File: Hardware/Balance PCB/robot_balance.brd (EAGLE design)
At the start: 100 x 50 mm, 49 parts, among them Q1 16Mhz

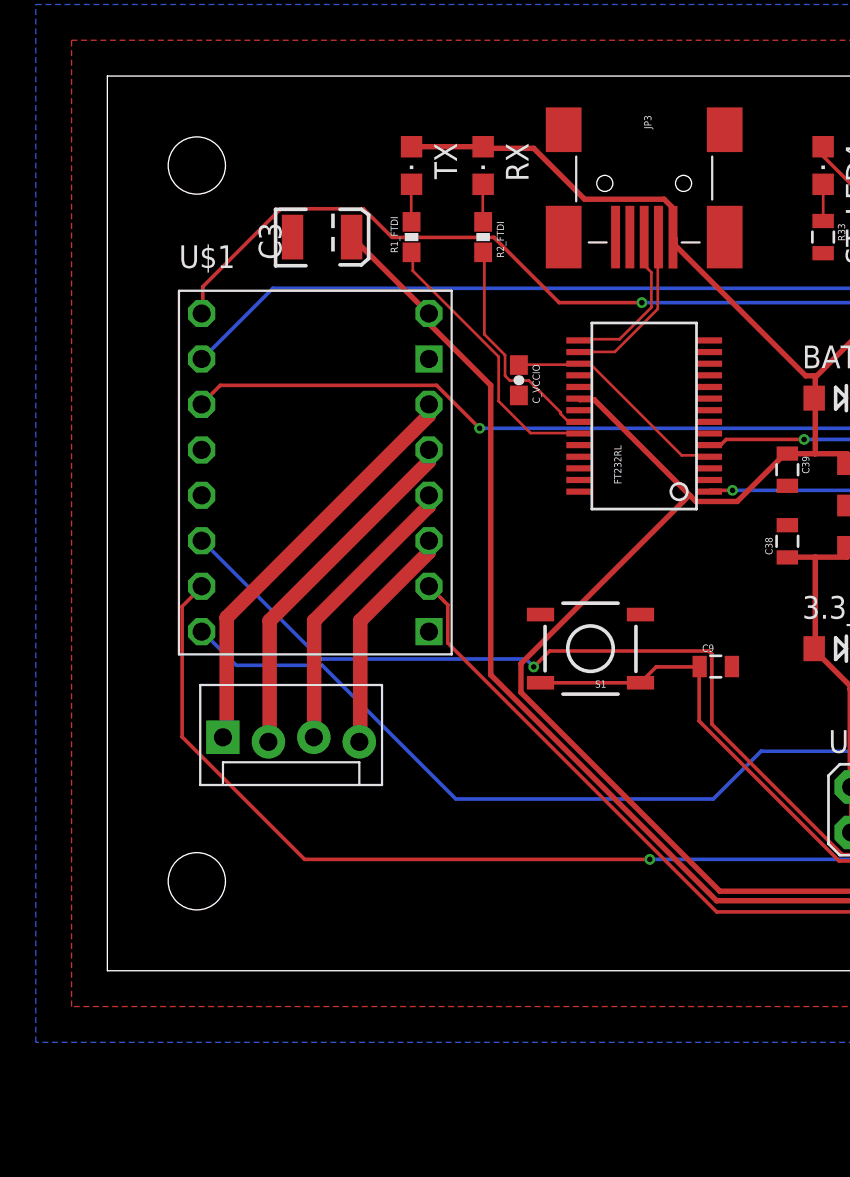
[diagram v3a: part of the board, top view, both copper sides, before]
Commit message: Micro usb instead of Mini
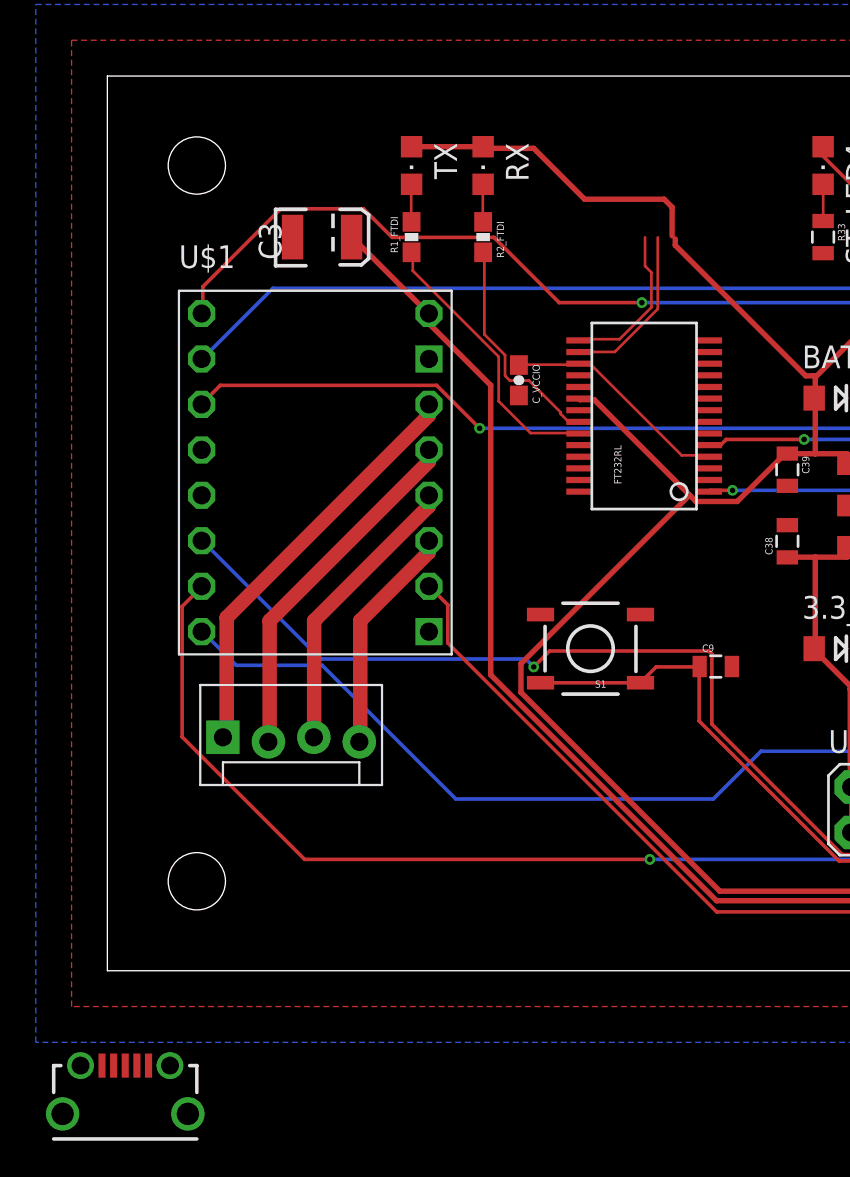
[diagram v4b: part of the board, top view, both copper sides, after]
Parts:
- removed JP3: USBOLD, SparkFun-Connectors:USB-MINIB-OLD
- added P1: 10118194-0001LF, usb_micro:10118194-0001LF
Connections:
- net 5V: now also P1.1; no longer JP3.VBUS
- net GND: now also P1.M1, P1.M2, P1.M3, P1.M4; no longer JP3.GND
- net USB_D+: now also P1.3; no longer JP3.D+
- net USB_D-: now also P1.2; no longer JP3.D-
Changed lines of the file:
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@@
 <attribute name="PROD_ID" value="CAP-08310" x="51.63" y="65.13" size="1.778" layer="27" display="off"/>
 </element>
-<element name="JP3" library="SparkFun-Connectors" package="USB-MINIB-OLD" value="USBOLD" x="30" y="44" rot="R270"/>
 <element name="JP4" library="SparkFun-Connectors" package="MOLEX-1X4_LOCK" value="" x="68" y="44" rot="R180"/>
 <element name="JP5" library="SparkFun-Connectors" package="MOLEX-1X4_LOCK" value="" x="72" y="6"/>
@@
 <element name="C_VCCIO" library="SparkFun-Capacitors" package="0603-CAP" value="0.1uF" x="23" y="33" rot="R270"/>
 <element name="U$2" library="JonathanLukas" package="2X10" value="JTAG_20PIN" x="53" y="9"/>
+<element name="P1" library="usb_micro" package="10118194-0001LF" value="10118194-0001LF" x="1" y="-8">
+<attribute name="MANPARTNO" value="10118194-0001LF" x="1" y="-8" size="1.778" layer="27" display="off"/>
+<attribute name="DISTRIBUTOR" value="Digikey" x="1" y="-8" size="1.778" layer="27" display="off"/>
+<attribute name="PARTNO" value="GT10040" x="1" y="-8" size="1.778" layer="27" display="off"/>
+<attribute name="MANUFACTURER" value="FCI" x="1" y="-8" size="1.778" layer="27" display="off"/>
+<attribute name="POPULATE" value="yes" x="1" y="-8" size="1.778" layer="27" display="off"/>
+<attribute name="DISTPARTNO" value="609-4618-1-ND" x="1" y="-8" size="1.778" layer="27" display="off"/>
+</element>
 </elements>
 <signals>
@@
 <vertex x="-2" y="-2"/>
 </polygon>
-<contactref element="JP3" pad="GND"/>
 <polygon width="0.1524" layer="16">
 <vertex x="-4" y="54"/>
@@
 <contactref element="U$2" pad="6"/>
 <contactref element="U$2" pad="4"/>
+<contactref element="P1" pad="M2"/>
+<contactref element="P1" pad="M4"/>
+<contactref element="P1" pad="M1"/>
+<contactref element="P1" pad="M3"/>
+<wire x1="86.81" y1="41" x2="94.97" y2="34.19" width="0" layer="19" extent="1-1"/>
+<wire x1="94.97" y1="18.95" x2="94.97" y2="34.19" width="0" layer="19" extent="1-1"/>
+<wire x1="76.9" y1="29" x2="86.81" y2="41" width="0" layer="19" extent="1-1"/>
+<wire x1="76.9" y1="26" x2="76.9" y2="29" width="0" layer="19" extent="1-1"/>
+<wire x1="72" y1="35.9" x2="76.9" y2="29" width="0" layer="19" extent="1-1"/>
+<wire x1="63" y1="35.9" x2="72" y2="35.9" width="0" layer="19" extent="1-1"/>
+<wire x1="62.75" y1="30.8" x2="63" y2="35.9" width="0" layer="19" extent="1-1"/>
+<wire x1="60.15" y1="23.25" x2="62.75" y2="30.8" width="0" layer="19" extent="1-1"/>
+<wire x1="62.75" y1="19.2" x2="60.15" y2="23.25" width="0" layer="19" extent="1-1"/>
 <wire x1="63" y1="15.1" x2="62.75" y2="19.2" width="0" layer="19" extent="1-1"/>
+<wire x1="66" y1="15.1" x2="63" y2="15.1" width="0" layer="19" extent="1-1"/>
 <wire x1="70" y1="15.1" x2="66" y2="15.1" width="0" layer="19" extent="1-1"/>
-<wire x1="60.15" y1="23.25" x2="62.75" y2="19.2" width="0" layer="19" extent="1-1"/>
+<wire x1="73" y1="15.1" x2="70" y2="15.1" width="0" layer="19" extent="1-1"/>
 <wire x1="61.89" y1="10.27" x2="63" y2="15.1" width="0" layer="19" extent="1-1"/>
-<wire x1="62.75" y1="30.8" x2="63" y2="35.9" width="0" layer="19" extent="1-1"/>
-<wire x1="23" y1="32.15" x2="17.97" y2="34.19" width="0" layer="19" extent="1-1"/>
-<wire x1="26.344" y1="31.325" x2="23" y2="32.15" width="0" layer="19" extent="1-1"/>
+<wire x1="64.43" y1="10.27" x2="61.89" y2="10.27" width="0" layer="19" extent="1-1"/>
+<wire x1="59.35" y1="10.27" x2="61.89" y2="10.27" width="0" layer="19" extent="1-1"/>
+<wire x1="56.81" y1="10.27" x2="59.35" y2="10.27" width="0" layer="19" extent="1-1"/>
+<wire x1="54.27" y1="10.27" x2="56.81" y2="10.27" width="0" layer="19" extent="1-1"/>
+<wire x1="51.73" y1="10.27" x2="54.27" y2="10.27" width="0" layer="19" extent="1-1"/>
+<wire x1="49.19" y1="10.27" x2="51.73" y2="10.27" width="0" layer="19" extent="1-1"/>
+<wire x1="46.65" y1="10.27" x2="49.19" y2="10.27" width="0" layer="19" extent="1-1"/>
+<wire x1="44.11" y1="10.27" x2="46.65" y2="10.27" width="0" layer="19" extent="1-1"/>
+<wire x1="55.1" y1="18" x2="60.15" y2="23.25" width="0" layer="19" extent="1-1"/>
+<wire x1="53" y1="20.1" x2="55.1" y2="18" width="0" layer="19" extent="1-1"/>
+<wire x1="52.2" y1="24.9" x2="53" y2="20.1" width="0" layer="19" extent="1-1"/>
+<wire x1="53.8" y1="27.1" x2="52.2" y2="24.9" width="0" layer="19" extent="1-1"/>
+<wire x1="53" y1="31.9" x2="53.8" y2="27.1" width="0" layer="19" extent="1-1"/>
+<wire x1="47.9" y1="32" x2="53" y2="31.9" width="0" layer="19" extent="1-1"/>
+<wire x1="47.9" y1="18" x2="53" y2="20.1" width="0" layer="19" extent="1-1"/>
+<wire x1="48" y1="40.1" x2="47.9" y2="32" width="0" layer="19" extent="1-1"/>
+<wire x1="52" y1="40.1" x2="48" y2="40.1" width="0" layer="19" extent="1-1"/>
+<wire x1="44" y1="40.1" x2="48" y2="40.1" width="0" layer="19" extent="1-1"/>
+<wire x1="40" y1="40.1" x2="44" y2="40.1" width="0" layer="19" extent="1-1"/>
+<wire x1="41.9012" y1="26" x2="47.9" y2="32" width="0" layer="19" extent="1-1"/>
+<wire x1="38" y1="27.1" x2="41.9012" y2="26" width="0" layer="19" extent="1-1"/>
+<wire x1="38" y1="24.9" x2="38" y2="27.1" width="0" layer="19" extent="1-1"/>
+<wire x1="33.656" y1="30.675" x2="38" y2="27.1" width="0" layer="19" extent="1-1"/>
+<wire x1="26.344" y1="31.325" x2="33.656" y2="30.675" width="0" layer="19" extent="1-1"/>
 <wire x1="26.344" y1="33.275" x2="26.344" y2="31.325" width="0" layer="19" extent="1-1"/>
 <wire x1="26.344" y1="28.725" x2="26.344" y2="31.325" width="0" layer="19" extent="1-1"/>
+<wire x1="26.344" y1="28.075" x2="26.344" y2="28.725" width="0" layer="19" extent="1-1"/>
+<wire x1="23" y1="32.15" x2="26.344" y2="31.325" width="0" layer="19" extent="1-1"/>
+<wire x1="17.97" y1="34.19" x2="23" y2="32.15" width="0" layer="19" extent="1-1"/>
+<wire x1="24.206" y1="19.905" x2="26.344" y2="28.075" width="0" layer="19" extent="1-1"/>
 <wire x1="29.794" y1="19.905" x2="24.206" y2="19.905" width="0" layer="19" extent="1-1"/>
-<wire x1="44" y1="40.1" x2="48" y2="40.1" width="0" layer="19" extent="1-1"/>
-<wire x1="53" y1="31.9" x2="47.9" y2="32" width="0" layer="19" extent="1-1"/>
-<wire x1="53.8" y1="27.1" x2="53" y2="31.9" width="0" layer="19" extent="1-1"/>
-<wire x1="33.656" y1="30.675" x2="38" y2="27.1" width="0" layer="19" extent="1-1"/>
-<wire x1="76.9" y1="29" x2="72" y2="35.9" width="0" layer="19" extent="1-1"/>
+<wire x1="34.9" y1="17" x2="29.794" y2="19.905" width="0" layer="19" extent="1-1"/>
+<wire x1="17.97" y1="18.95" x2="24.206" y2="19.905" width="0" layer="19" extent="1-1"/>
+<wire x1="60.38" y1="44.127" x2="63" y2="35.9" width="0" layer="19" extent="1-1"/>
+<wire x1="10.35" y1="41" x2="17.97" y2="34.19" width="0" layer="19" extent="1-1"/>
+<wire x1="79.62" y1="5.873" x2="73" y2="15.1" width="0" layer="19" extent="1-1"/>
+<wire x1="3.5" y1="-5.3" x2="17.97" y2="18.95" width="0" layer="19" extent="1-1"/>
+<wire x1="4.5" y1="-8" x2="3.5" y2="-5.3" width="0" layer="19" extent="1-1"/>
+<wire x1="-1.5" y1="-5.3" x2="3.5" y2="-5.3" width="0" layer="19" extent="1-1"/>
+<wire x1="-2.5" y1="-8" x2="-1.5" y2="-5.3" width="0" layer="19" extent="1-1"/>
 </signal>
 <signal name="3.3V" class="3">
@@
 <signal name="USB_D-" class="1">
 <contactref element="FT232RL" pad="16"/>
-<contactref element="JP3" pad="D-"/>
 <wire x1="28.3591" y1="34.5821" x2="26.4033" y2="34.5821" width="0.1524" layer="1"/>
 <wire x1="30.7594" y1="36.9824" x2="28.3591" y2="34.5821" width="0.1524" layer="1"/>
 <wire x1="30.7594" y1="40.9829" x2="30.7594" y2="36.9824" width="0.1524" layer="1"/>
 <wire x1="26.4033" y1="34.5821" x2="26.344" y2="34.575" width="0.1524" layer="1"/>
-<wire x1="30.7594" y1="40.9829" x2="30.8" y2="41" width="0.1524" layer="1"/>
+<contactref element="P1" pad="2"/>
+<wire x1="0.35" y1="-5.3" x2="26.344" y2="34.575" width="0" layer="19" extent="1-1"/>
 </signal>
 <signal name="USB_D+" class="1">
 <contactref element="FT232RL" pad="15"/>
-<contactref element="JP3" pad="D+"/>
 <wire x1="28.6258" y1="35.2933" x2="26.4033" y2="35.2933" width="0.1524" layer="1"/>
 <wire x1="30.4038" y1="37.0713" x2="28.6258" y2="35.2933" width="0.1524" layer="1"/>
@@
 <wire x1="30.0482" y1="40.9829" x2="30.0482" y2="39.3827" width="0.1524" layer="1"/>
 <wire x1="26.4033" y1="35.2933" x2="26.344" y2="35.225" width="0.1524" layer="1"/>
-<wire x1="30.0482" y1="40.9829" x2="30" y2="41" width="0.1524" layer="1"/>
+<contactref element="P1" pad="3"/>
+<wire x1="1" y1="-5.3" x2="26.344" y2="35.225" width="0" layer="19" extent="1-1"/>
 </signal>
 <signal name="5V" class="3">
@@
 <contactref element="C39" pad="1"/>
 <contactref element="U$7" pad="1"/>
-<contactref element="JP3" pad="VBUS"/>
 <contactref element="BATT_PWR" pad="A"/>
 <contactref element="JP4" pad="3"/>
@@
 <wire x1="31.5595" y1="41.0718" x2="31.5595" y2="42.672" width="0.3048" layer="1"/>
 <wire x1="21.0693" y1="45.9613" x2="21" y2="46.05" width="0.3048" layer="1"/>
-<wire x1="31.5595" y1="41.0718" x2="31.61" y2="40.99" width="0.3048" layer="1"/>
 <wire x1="41.3385" y1="28.8925" x2="39.5605" y2="28.8925" width="0.3048" layer="1"/>
 <wire x1="39.5605" y1="28.8925" x2="38.0492" y2="28.8925" width="0.3048" layer="1"/>
@@
 <wire x1="39.0271" y1="33.2486" x2="31.7373" y2="40.5384" width="0.3048" layer="1"/>
 <wire x1="39.4716" y1="33.2486" x2="39.0271" y2="33.2486" width="0.3048" layer="1"/>
-<wire x1="31.7373" y1="40.894" x2="31.61" y2="40.99" width="0.3048" layer="1"/>
 <wire x1="39.4716" y1="33.2486" x2="39.5605" y2="33.1597" width="0.3048" layer="1"/>
+<contactref element="P1" pad="1"/>
+<wire x1="31.7373" y1="40.894" x2="31.5595" y2="41.0718" width="0" layer="19" extent="1-1"/>
+<wire x1="-0.3" y1="-5.3" x2="23.114" y2="15.5575" width="0" layer="19" extent="1-1"/>
 </signal>
 <signal name="N$9" class="1">

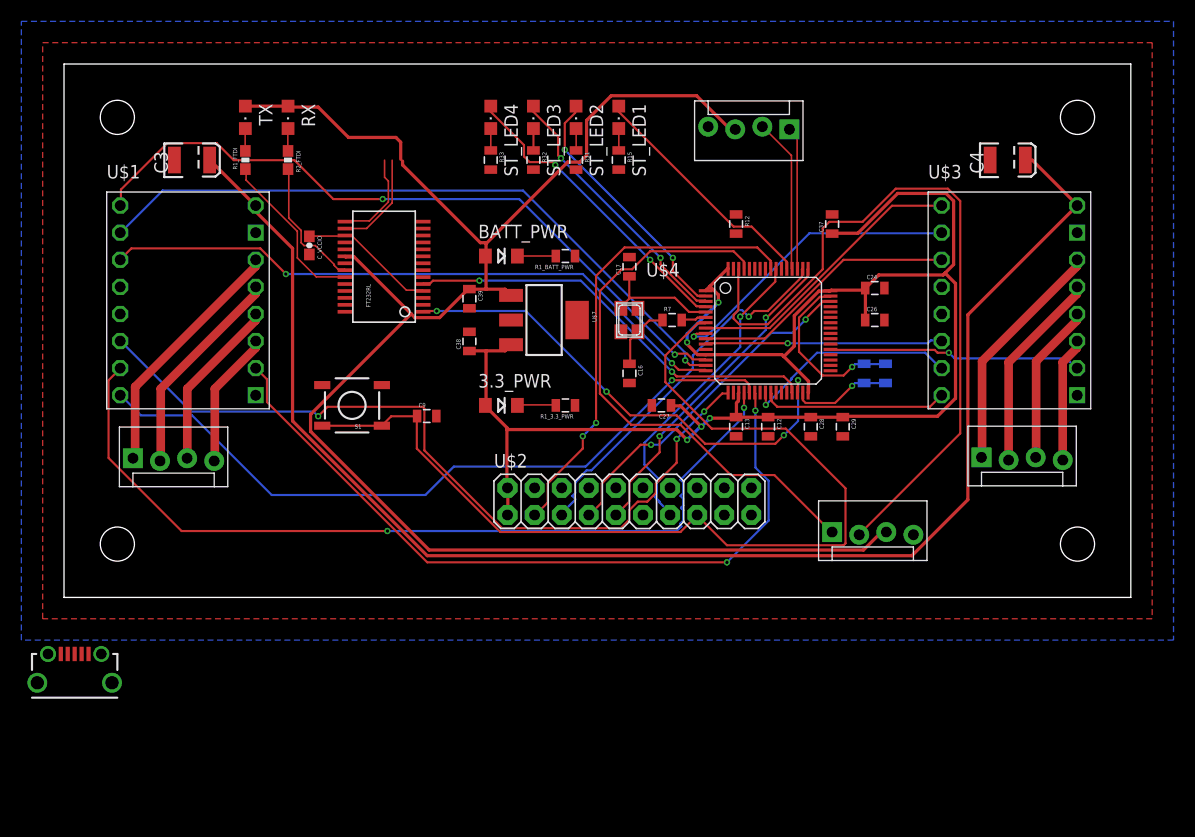
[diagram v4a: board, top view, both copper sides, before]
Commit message: reserving audio pins
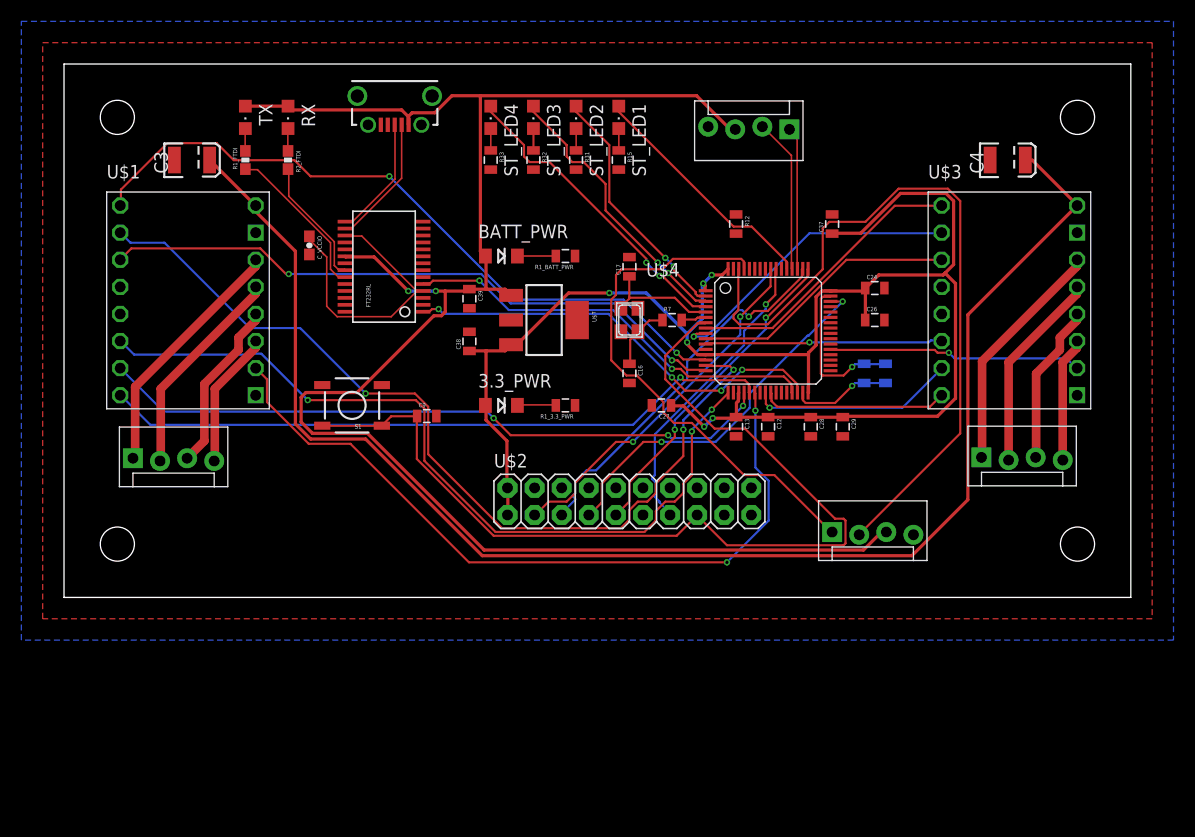
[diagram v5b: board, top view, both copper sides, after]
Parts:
- moved P1 62.6 mm to (31.0, 47.0), turned to 180 degrees
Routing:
- net S1_M0: track 63.7 -> 83.5 mm, vias 1 -> 3
- net S1_STEP: track 81.2 -> 63.6 mm, vias 2 -> 3
- net N$13: track 12.9 -> 27.1 mm
- net !JTRST: track 43.6 -> 34.2 mm
- net 5V: track 159.0 -> 166.5 mm, vias 0 -> 2
- net UART3_RX: track 46.3 -> 40.5 mm
- net S1_DIR: track 68.3 -> 63.0 mm
- net IMU_SCL: track 52.9 -> 49.5 mm
- net SWDIO: track 32.0 -> 35.0 mm
- net USB_D-: track 9.41 -> 12.3 mm
- net USB_D+: track 8.89 -> 11.4 mm
- net N$12: track 16.5 -> 14.7 mm
- net !S1_SLEEP: track 74.9 -> 76.3 mm
- net 3.3V: track 150.0 -> 151.3 mm, vias 5 -> 6
- net S2_STEP: track 20.4 -> 19.3 mm
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
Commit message: changed inter-board connect to 6 pin and added enable line
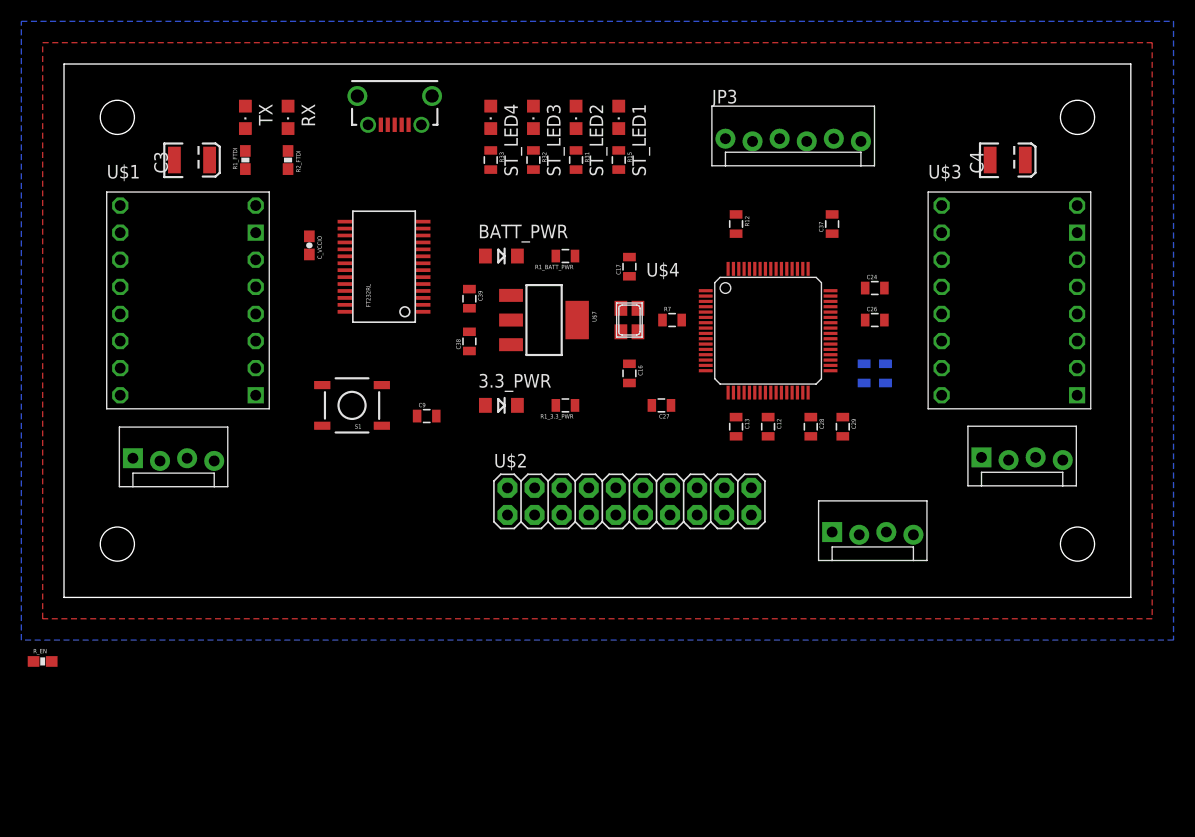
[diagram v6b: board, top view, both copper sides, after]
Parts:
- removed JP4: (no value), SparkFun-Connectors:MOLEX-1X4_LOCK
- added JP3: (no value), SparkFun-Connectors:MOLEX-1X6_LOCK
- added R_EN: 1K, SparkFun-Passives:0603-RES
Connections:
- new net ENABLE: JP3.1, R_EN.1
- new net N$6: R_EN.2, U$4.40
- net 3.3V: now also JP3.5
- net 5V: now also JP3.6; no longer JP4.3
- net ARDUINO_RX: now also JP3.2; no longer JP4.2
- net ARDUINO_TX: now also JP3.3; no longer JP4.1
- net GND: now also JP3.4, P1.5; no longer JP4.4
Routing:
- net 5V: track 166.5 -> 0.00 mm, vias 2 -> 0
- net 3.3V: track 151.3 -> 0.00 mm, vias 6 -> 0
- net V_USB: track 136.9 -> 0.00 mm
- net !RST: track 90.3 -> 0.00 mm
- net S1_M0: track 83.5 -> 0.00 mm, vias 3 -> 0
- net !S1_SLEEP: track 76.3 -> 0.00 mm, vias 3 -> 0
- net !S1_FAULT: track 71.0 -> 0.00 mm, vias 2 -> 0
- net IMU_SDA: track 69.5 -> 0.00 mm
- net !S1_ENABLE: track 66.6 -> 0.00 mm, vias 2 -> 0
- net S1_STEP: track 63.6 -> 0.00 mm, vias 3 -> 0
- net S1_DIR: track 63.0 -> 0.00 mm, vias 1 -> 0
- net S1_M1: track 60.1 -> 0.00 mm, vias 2 -> 0
- net IMU_SCL: track 49.5 -> 0.00 mm
- net UART3_RX: track 40.5 -> 0.00 mm, vias 4 -> 0
- net UART3_TX: track 39.5 -> 0.00 mm, vias 2 -> 0
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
